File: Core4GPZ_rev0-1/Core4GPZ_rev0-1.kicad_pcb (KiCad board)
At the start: 2 copper layers, 91.4 x 105.4 mm, 39 parts, among them IC1 MAX9926UAEE_V+, M3 MountingHole_3.2mm_M3_DIN965_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, Q1 FGP3440G2-F085, Q2 FGP3440G2-F085, U2 core4, U3 MPXHZ6250AC6T1

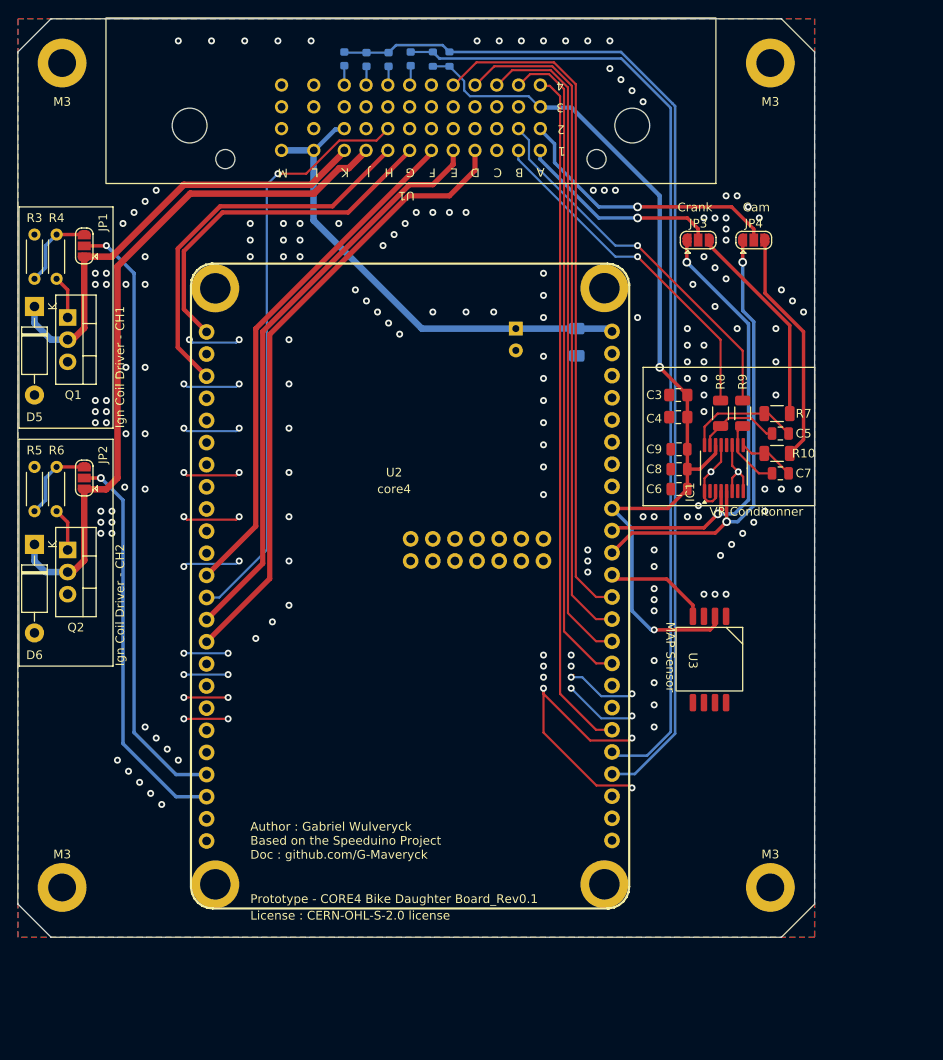
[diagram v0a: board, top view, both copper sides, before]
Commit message: Implemented DRV8825 and upgrade IGN Driver
Ignition drivers upgraded with SMD IGBT FGD3440
Added Stepper Driver DRV8825
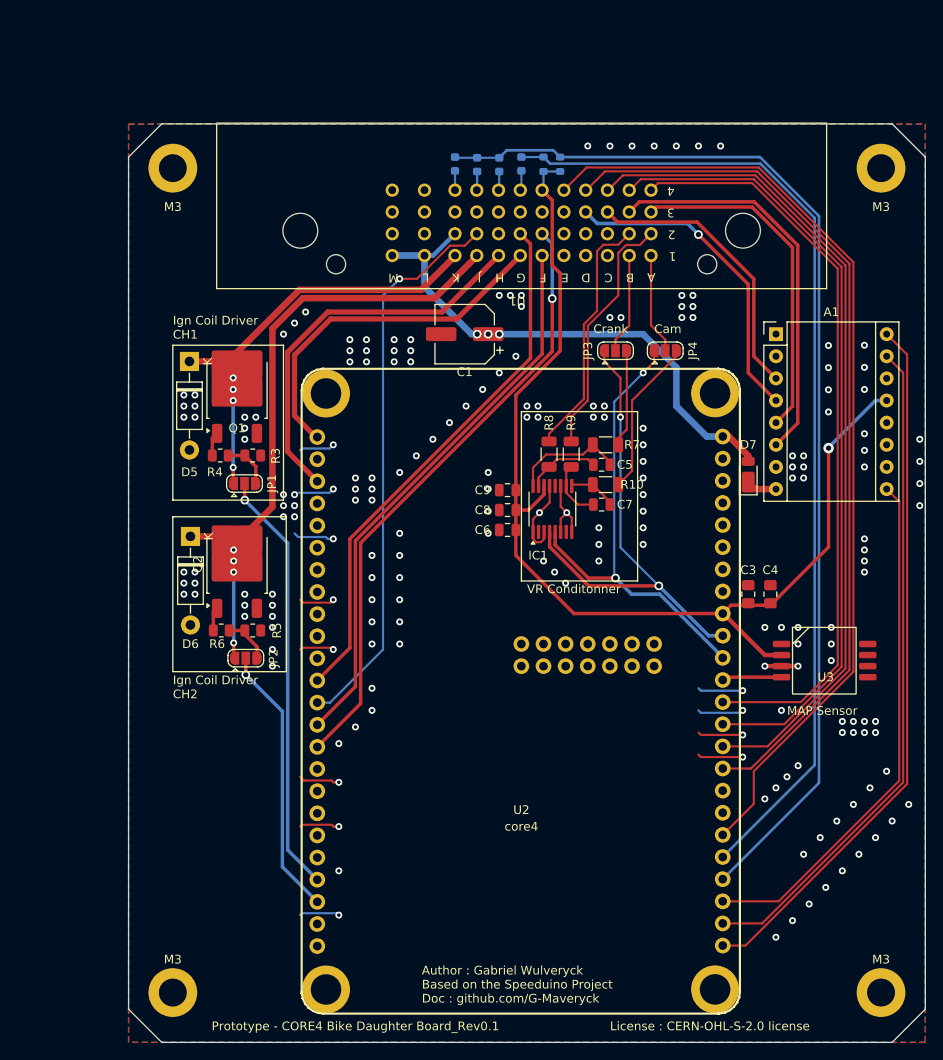
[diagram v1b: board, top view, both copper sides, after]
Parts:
- removed C2: 100nF, Capacitor_SMD:C_1206_3216Metric_Pad1.33x1.80mm_HandSolder
- added A1: Pololu_Breakout_DRV8825, Module:Pololu_Breakout-16_15.2x20.3mm, F.Cu at (146.1, 62.9)
- added D7: D_Schottky, Diode_SMD:D_PowerDI-123, F.Cu at (142.9, 79.0)
- C1: value 10uF -> 100uF; footprint Capacitor_THT:CP_Radial_D5.0mm_P2.50mm -> Capacitor_SMD:CP_Elec_6.3x7.7; moved to F.Cu
- Q1, Q2: value FGP3440G2-F085 -> FGD3440G2-F085; footprint Package_TO_SOT_THT:TO-220-3_Vertical -> Package_TO_SOT_SMD:TO-252-2
- R3, R4, R5, R6: footprint Resistor_THT:R_Axial_DIN0204_L3.6mm_D1.6mm_P5.08mm_Horizontal -> Resistor_SMD:R_0805_2012Metric
- moved JP1 32.9 mm to (85.1, 80.0), turned to 0 degrees
- moved R3 32.2 mm to (86.0, 76.8), turned to 180 degrees
- moved R5 28.5 mm to (86.0, 96.9), turned to 180 degrees
- moved JP2 27.8 mm to (85.2, 100.0), turned to 0 degrees
- moved R4 27.6 mm to (82.3, 76.8), turned to 0 degrees
- moved C3 24.2 mm to (142.9, 92.7), turned to 90 degrees
- moved R6 23.3 mm to (82.4, 96.9), turned to 0 degrees
- moved C4 22.9 mm to (145.4, 92.7), turned to 90 degrees
- moved Q1 21.1 mm to (84.2, 69.2), turned to 90 degrees
- moved C5 20.8 mm to (126.0, 77.9)
- moved C7 20.8 mm to (126.0, 82.4)
- moved C6 20.2 mm to (115.3, 85.3)
- moved C8 20.2 mm to (115.3, 83.1)
- moved C9 20.2 mm to (115.3, 80.8)
- moved R9 20.2 mm to (122.6, 76.6)
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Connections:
- C1 pad 2: BIKE_GROUND -> GND
- C3 pad 2: BIKE_GROUND -> GND
- C4 pad 2: BIKE_GROUND -> GND
- C6 pad 2: BIKE_GROUND -> GND
- C8 pad 2: BIKE_GROUND -> GND
- C9 pad 2: BIKE_GROUND -> GND
- D5 pad 2: BIKE_GROUND -> GND
- D6 pad 2: BIKE_GROUND -> GND
- IC1 pad 1: BIKE_GROUND -> GND
- IC1 pad 11: BIKE_GROUND -> GND
- IC1 pad 13: BIKE_GROUND -> GND
- IC1 pad 3: BIKE_GROUND -> GND
- IC1 pad 6: BIKE_GROUND -> GND
- IC1 pad 8: BIKE_GROUND -> GND
- M3 pad 1: BIKE_GROUND -> GND (x4)
- Q1 pad 3: BIKE_GROUND -> GND
- Q2 pad 3: BIKE_GROUND -> GND
- R3 pad 1: Net-(JP1-B) -> GND
- R3 pad 2: BIKE_GROUND -> Net-(JP1-B)
- R5 pad 1: Net-(JP2-B) -> GND
- R5 pad 2: BIKE_GROUND -> Net-(JP2-B)
- U1 pad 1: CRANK_SNSR -> CAM_SNSR
- U1 pad 11: CAM_SNSR -> CAM_SNSR_VR-
- U1 pad 12: CAM_SNSR_VR- -> CRANK_SNSR_VR-
- U1 pad 16: unconnected-(U1A-2F-Pad16) -> /FAN_CTL
- U1 pad 17: unconnected-(U1A-2G-Pad17) -> /IDLE_1
- U1 pad 18: /TACHO -> unconnected-(U1A-2H-Pad18)
- U1 pad 19: unconnected-(U1A-2J-Pad19) -> /TACHO_OUT
- U1 pad 2: CRANK_SNSR_VR- -> CRANK_SNSR
- U1 pad 21: SNSR_+5V -> Stepper_B1
- U1 pad 22: unconnected-(U1B-3B-Pad22) -> Stepper_B2
- U1 pad 23: unconnected-(U1B-3C-Pad23) -> Stepper_A2
- U1 pad 24: unconnected-(U1B-3D-Pad24) -> Stepper_A1
- U1 pad 31: /FLEX_SNSR -> /TPS_SNSR
- U1 pad 32: /02_SNSR -> /CLT_SNSR
- U1 pad 34: /CLT_SNSR -> /02_SNSR
- U1 pad 35: /TPS_SNSR -> /FLEX_SNSR
- U1 pad 36: unconnected-(U1B-4F-Pad36) -> SNSR_+5V
- U1 pad 4: /FAN_CTL -> unconnected-(U1A-1D-Pad4)
- U1 pad 43: BIKE_GROUND -> GND
- U1 pad 44: BIKE_GROUND -> GND
- U1 pad 45: BIKE_GROUND -> GND
- U1 pad 46: BIKE_GROUND -> GND
- U1 pad 47: BIKE_GROUND -> GND
- U1 pad 48: BIKE_GROUND -> GND
- U1 pad 5: /FUEL_PUMP -> unconnected-(U1A-1E-Pad5)
- U1 pad 6: /IDLE_1 -> /FUEL_PUMP
- U2 pad 100: BIKE_GROUND -> (no net)
- U2 pad 101: BIKE_GROUND -> (no net)
- U2 pad 102: BIKE_GROUND -> (no net)
- U2 pad 103: BIKE_GROUND -> (no net)
- U2 pad 13: /TACHO -> /TACHO_OUT
- U2 pad 23: IGN_TRIG_3 -> unconnected-(U2A-IGN3-Pad23)
- U2 pad 24: IGN_TRIG_4 -> unconnected-(U2A-IGN4-Pad24)
- U2 pad 26: BIKE_GROUND -> GND
- U2 pad 27: BIKE_GROUND -> GND
- U2 pad 28: BIKE_GROUND -> GND
- U2 pad 29: BIKE_GROUND -> GND
- U2 pad 30: BIKE_GROUND -> GND
- U2 pad 31: BIKE_GROUND -> GND
- U2 pad 32: BIKE_GROUND -> GND
- U2 pad 46: unconnected-(U2B-ENBL-Pad46) -> /EN
- U2 pad 47: unconnected-(U2B-STEP-Pad47) -> /STEP
- U2 pad 48: unconnected-(U2B-DIR-Pad48) -> /DIR
- U2 pad 5: /INJ3_TRIG -> unconnected-(U2A-INJ3-Pad5)
- U2 pad 61: BIKE_GROUND -> GND
- U2 pad 7: /INJ4_TRIG -> unconnected-(U2A-INJ4-Pad7)
- U3 pad 3: BIKE_GROUND -> GND
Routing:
- net BIKE_GROUND: track 124.9 -> 0.00 mm, vias 194 -> 0
- net /DIR: track 0.00 -> 81.4 mm
- net GND: track 0.00 -> 78.1 mm, vias 0 -> 196
- net /STEP: track 0.00 -> 77.1 mm
- net /TACHO: track 67.6 -> 0.00 mm, vias 1 -> 0
- net /TACHO_OUT: track 0.00 -> 64.4 mm, vias 0 -> 1
- net /EN: track 0.00 -> 60.1 mm
- net Stepper_B2: track 0.00 -> 45.8 mm
- net Stepper_B1: track 0.00 -> 39.4 mm
- net Stepper_A1: track 0.00 -> 36.8 mm, vias 0 -> 1
- net Stepper_A2: track 0.00 -> 32.5 mm
- net /FLEX_SNSR: track 79.0 -> 110.9 mm
- net /02_SNSR: track 75.8 -> 101.5 mm
- net IGN_TRIG_1: track 70.4 -> 49.1 mm
- net /IAT_SNSR: track 76.5 -> 96.4 mm
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- added copper zone on B.Cu, net GND
- added copper zone on F.Cu, net GND
- removed copper zone on B.Cu, net BIKE_GROUND
- removed copper zone on F.Cu, net BIKE_GROUND
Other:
- board text added: "Ign Coil Driver CH1"
- board text added: "Ign Coil Driver CH2"
- board text removed: "Ign Coil Driver - CH1"
- board text removed: "Ign Coil Driver - CH2"

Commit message: Reduced board width
moved IGN Driver under the Core4 to reduce overall board size
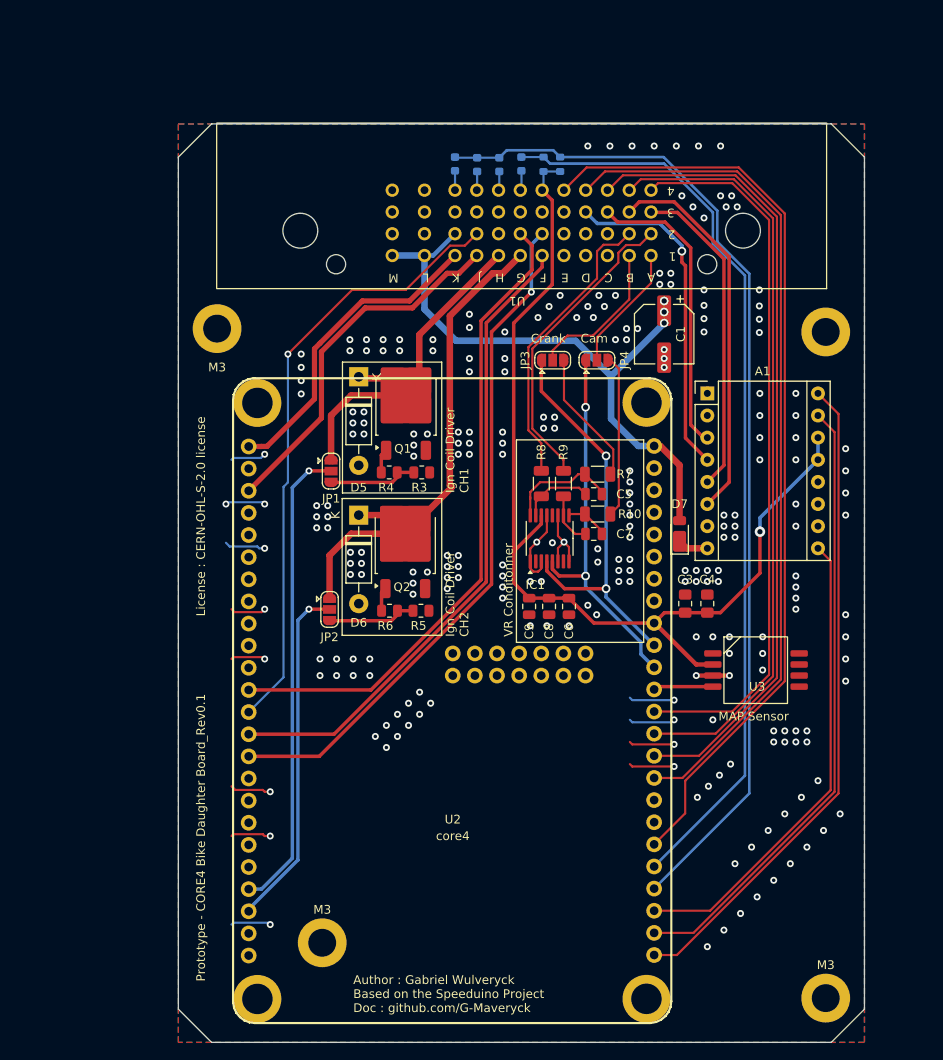
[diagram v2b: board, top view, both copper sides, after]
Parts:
- moved C1 22.9 mm to (133.2, 62.9), turned to -90 degrees
- moved M3 19.8 mm to (151.8, 62.6)
- moved D5 19.5 mm to (98.2, 67.8)
- moved Q1 19.5 mm to (103.6, 71.2)
- moved R3 19.5 mm to (105.4, 78.7)
- moved R4 19.5 mm to (101.7, 78.7)
- moved D6 19.5 mm to (98.2, 83.6)
- moved Q2 19.4 mm to (103.5, 87.0)
- moved R5 19.4 mm to (105.3, 94.6)
- moved R6 19.4 mm to (101.7, 94.6)
- moved M3 19.1 mm to (81.9, 62.2)
- moved M3 18.1 mm to (94.0, 132.7)
- moved C9 13.6 mm to (117.7, 94.1), turned to -90 degrees
- moved C8 12.0 mm to (120.0, 94.1), turned to -90 degrees
- moved C6 11.3 mm to (122.3, 94.1), turned to -90 degrees
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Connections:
- U1 pad 10: IGN_COIL1_DRIVE -> /INJ1_TRIG
- U1 pad 7: /INJ1_TRIG -> IGN_COIL2_DRIVE
- U1 pad 8: /INJ2_TRIG -> IGN_COIL1_DRIVE
- U1 pad 9: IGN_COIL2_DRIVE -> /INJ2_TRIG
- U2 pad 100: (no net) -> GND
- U2 pad 101: (no net) -> GND
- U2 pad 102: (no net) -> GND
- U2 pad 103: (no net) -> GND
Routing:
- net /IDLE_1: track 61.9 -> 74.6 mm
- net IGN_COIL2_DRIVE: track 73.6 -> 62.1 mm, vias 4 -> 0
- net BIKE_+12V_SWITCHED_IN: track 60.4 -> 71.6 mm
- net CAM_SIGNAL: track 54.2 -> 43.5 mm
- net IGN_COIL1_DRIVE: track 53.7 -> 43.4 mm, vias 4 -> 0
- net /FUEL_PUMP: track 64.5 -> 74.6 mm
- net CRANK_SIGNAL: track 55.8 -> 46.8 mm
- net SAFE_SIGNAL: track 126.0 -> 117.2 mm
- net NEUTRAL_SIGNAL: track 114.3 -> 105.5 mm
- net IGN_TRIG_2: track 31.4 -> 39.9 mm
- net /FAN_CTL: track 70.5 -> 78.7 mm
- net SNSR_+5V: track 124.9 -> 117.7 mm
- net CAM_SNSR_VR-: track 28.5 -> 35.3 mm
- net CRANK_SNSR: track 11.8 -> 18.0 mm
- net /TACHO_OUT: track 64.4 -> 70.3 mm
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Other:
- board size 91.4 x 105.4 mm -> 78.7 x 105.4 mm

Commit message: Minor visual modifications
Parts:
- moved C6 1.53 mm to (120.8, 94.0)
- moved C8 1.53 mm to (118.5, 94.0)
- moved C9 1.53 mm to (116.2, 94.0)
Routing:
- net SNSR_+5V: track 117.7 -> 120.4 mm
- net GND: vias 242 -> 257

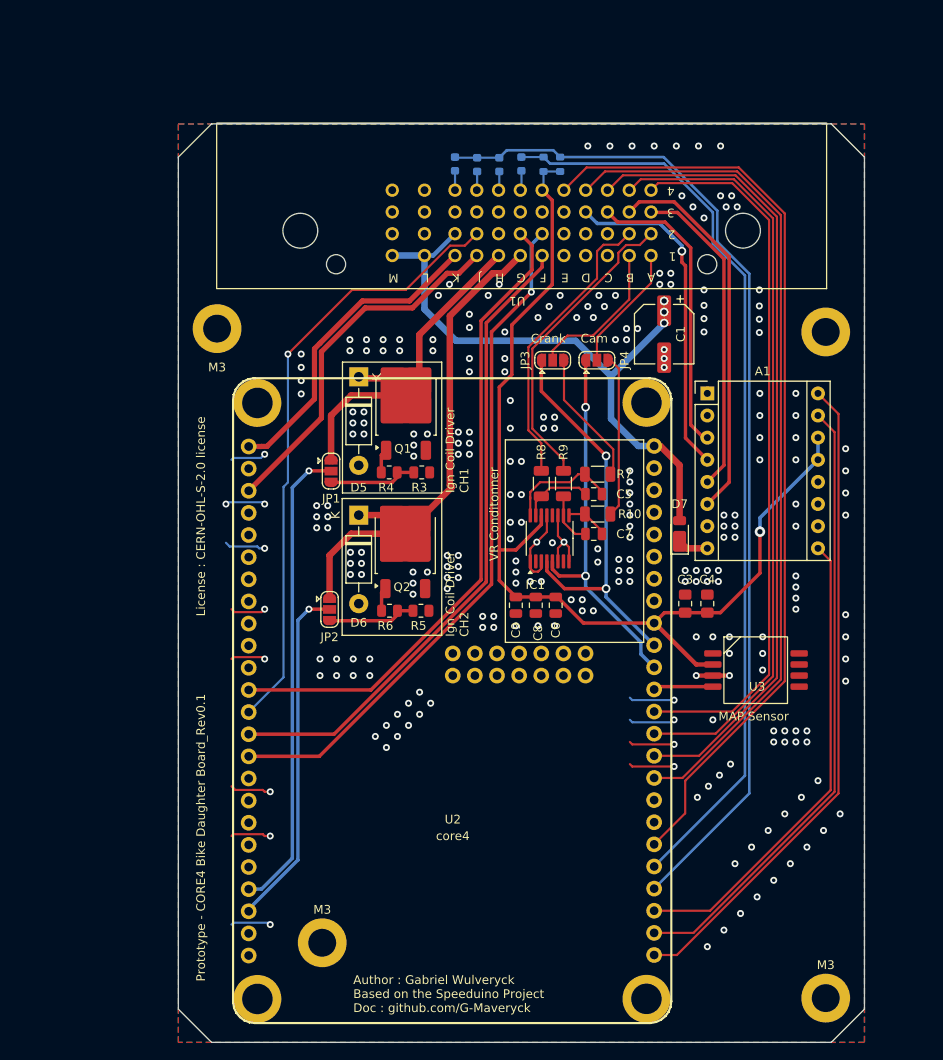
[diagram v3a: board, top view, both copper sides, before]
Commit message: Added AOP for a proper decoupling for CLT
Modified Fixing point and dimensions on the enclosure
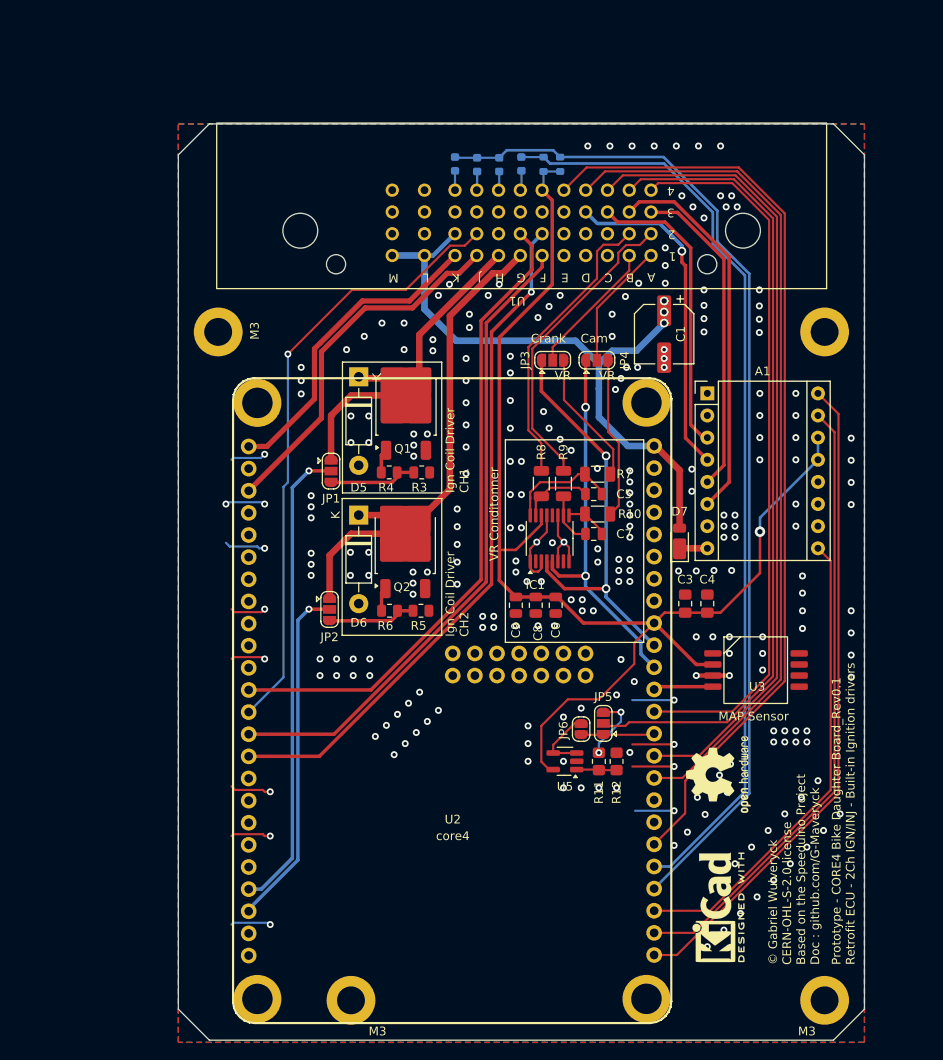
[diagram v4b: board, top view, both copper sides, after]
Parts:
- added JP5: SolderJumper_3_Open, Jumper:SolderJumper-3_P1.3mm_Open_RoundedPad1.0x1.5mm, F.Cu at (126.2, 107.5)
- added JP6: SolderJumper_2_Open, Jumper:SolderJumper-2_P1.3mm_Open_RoundedPad1.0x1.5mm, F.Cu at (123.7, 108.2)
- added R11: 660k, Resistor_SMD:R_0805_2012Metric_Pad1.20x1.40mm_HandSolder, F.Cu at (125.7, 111.9)
- added R12: 300K, Resistor_SMD:R_0805_2012Metric_Pad1.20x1.40mm_HandSolder, F.Cu at (127.8, 111.9)
- added REF**: OSHW-Logo2_9.8x8mm_SilkScreen, Symbol:OSHW-Logo2_9.8x8mm_SilkScreen, F.Cu at (139.5, 113.4)
- added REF**: KiCad-Logo2_5mm_SilkScreen, Symbol:KiCad-Logo2_5mm_SilkScreen, F.Cu at (139.5, 128.7)
- added U5: LMV321, Package_TO_SOT_SMD:SOT-23-5_HandSoldering, F.Cu at (121.8, 111.9)
- moved M3 7.38 mm to (97.3, 139.3)
- moved D7 0.86 mm to (135.0, 86.7)
- moved M3 0.40 mm to (82.0, 62.6)
- moved M3 0.28 mm to (151.6, 139.3)
- moved M3 0.13 mm to (151.6, 62.6)
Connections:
- U2 pad 38: /CLT_SNSR -> /CLT_5V
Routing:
- net SNSR_+5V: track 120.4 -> 145.5 mm
- net /CLT_5V: track 0.00 -> 8.99 mm
- net Net-(JP6-B): track 0.00 -> 7.87 mm
- net Net-(JP5-B): track 0.00 -> 7.75 mm, vias 0 -> 2
- net /CLT_SNSR: track 87.9 -> 93.3 mm
- net Net-(U5-+): track 0.00 -> 4.60 mm
- net BIKE_+12V_SWITCHED_IN: track 71.6 -> 73.6 mm
- net GND: track 77.7 -> 75.7 mm, vias 257 -> 255
- net CRANK_SNSR: track 18.0 -> 16.3 mm
- net NEUTRAL_SIGNAL: track 105.5 -> 106.6 mm
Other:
- board size 78.7 x 105.4 mm -> 78.7 x 105.2 mm
- board text added: "Prototype - CORE4 Bike Daughter Board_Rev0.1 Retrofit ECU - 2Ch IGN/INJ - Built-in Ignition drivers"
- board text added: "VR"
- board text added: "© Gabriel Wulveryck CERN-OHL-S-2.0 license Based on the Speeduino Project Doc : github.com/G-Maveryck"
- board text removed: "Author : Gabriel Wulveryck Based on the Speeduino Project Doc : github.com/G-Maveryck"
- board text removed: "License : CERN-OHL-S-2.0 license"
- board text removed: "Prototype - CORE4 Bike Daughter Board_Rev0.1"
